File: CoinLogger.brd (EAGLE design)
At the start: 34.8 x 34.8 mm, 17 parts, among them IC1 TINY11S, U4 LIS331

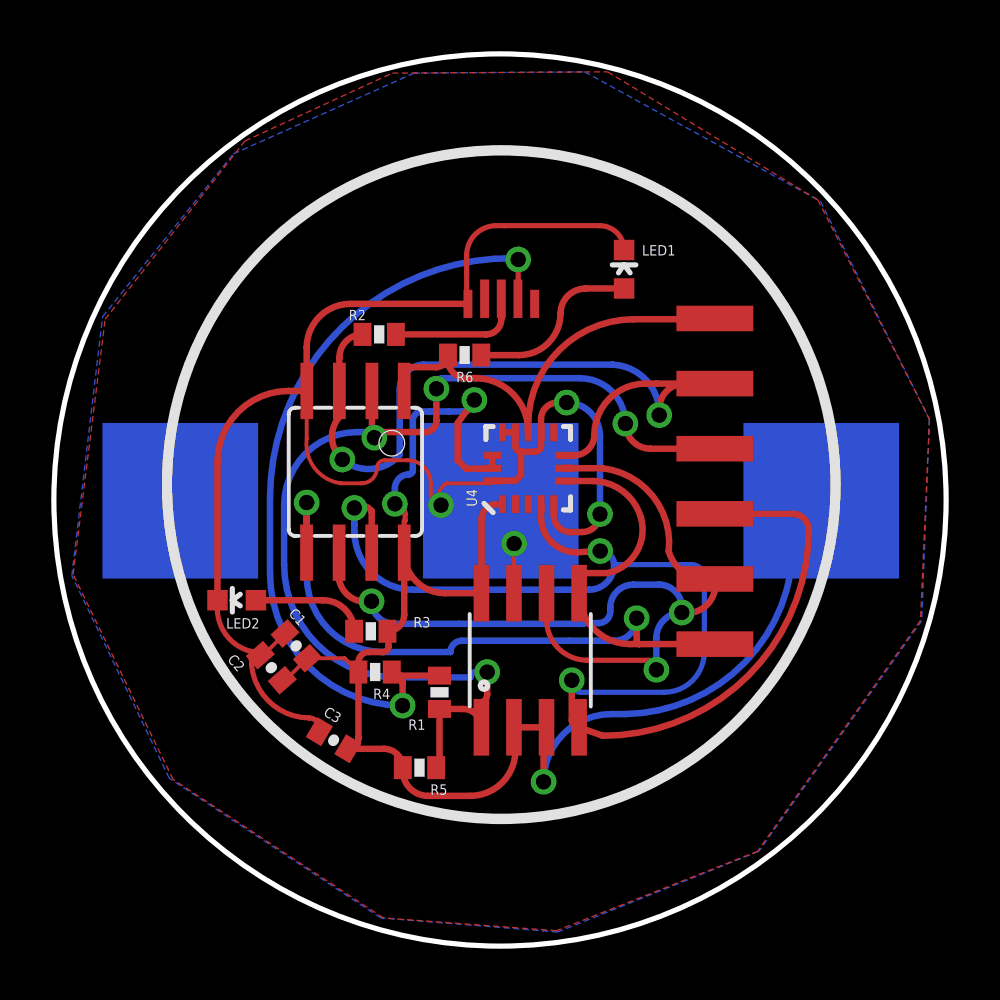
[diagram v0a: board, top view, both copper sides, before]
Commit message: Board is now v1.1
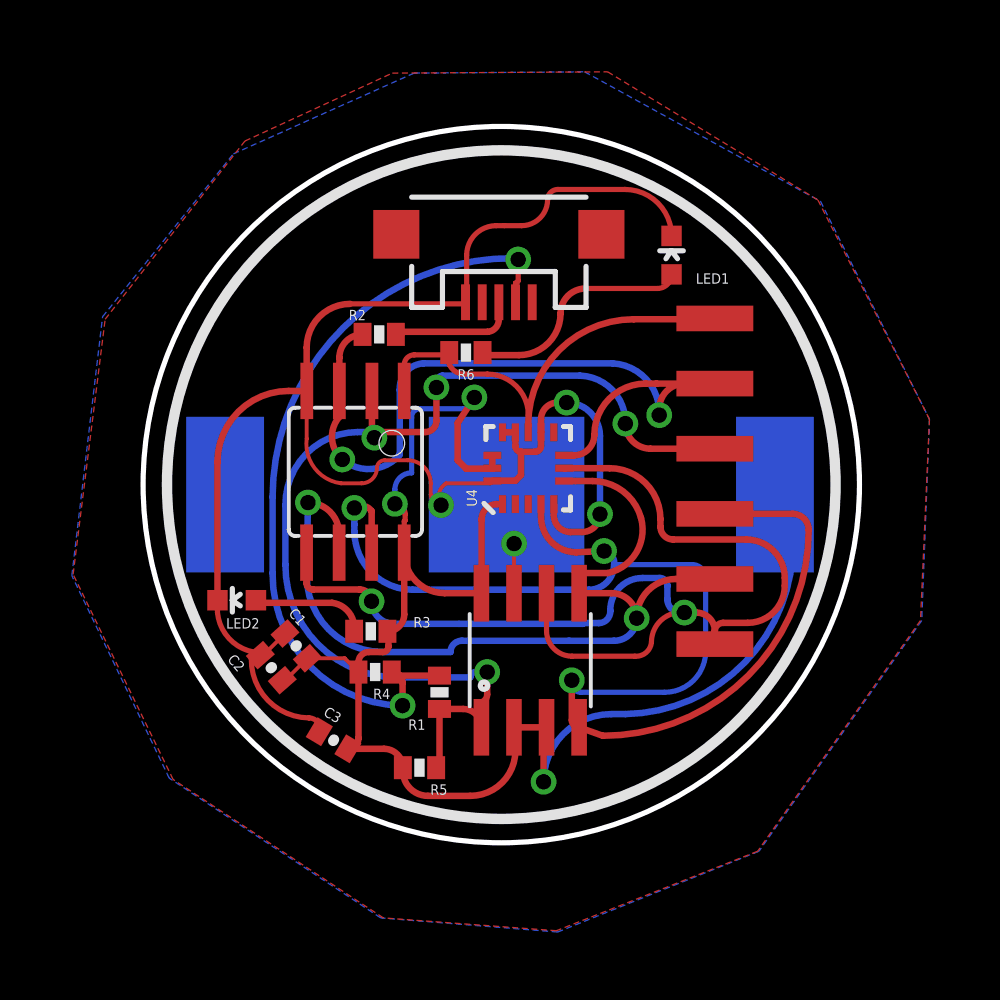
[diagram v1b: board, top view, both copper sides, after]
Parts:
- removed BAT2: (no value), SparkFun:BATTCON_20MM
- removed JP1: USB_MICROB_PLUG, SparkFun:MICRO-B-RA-SMT
- added BAT1: (no value), SparkFun:BATTCON_20MM
- added X1: USB-MICROB, SparkFun:USB-MICROB
- moved LED1 1.93 mm to (28.6, 46.0)
- moved R6 0.11 mm to (20.6, 42.2)
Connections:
- net GND: now also BAT1.2, X1.GND; no longer BAT2.2, JP1.5
- net N$2: now also X1.D+; no longer JP1.3
- net N$6: now also IC1.5, JP2.1; no longer IC1.6, JP2.2
- net N$7: now also IC1.6, JP2.2; no longer IC1.5, JP2.1
- net N$8: now also X1.D-; no longer JP1.2
- net VCC: now also BAT1.1; no longer BAT2.1
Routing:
- net N$6: track 34.9 -> 43.1 mm, vias 3 -> 2
- net N$10: track 6.65 -> 8.72 mm
- net VCC: track 61.1 -> 62.0 mm
- net N$12: track 17.5 -> 18.1 mm
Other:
- board size 34.8 x 34.8 mm -> 27.9 x 27.9 mm

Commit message: Lots of fixes, added NanoLogger
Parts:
- added R7: 4.7k, SparkFun:0402-RES
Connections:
- removed net N$11: IC1.3, JP2.5, R2.1, U4.8
- removed net N$12: IC1.1, JP2.6, R6.2, U4.11
- new net N$13: IC1.3, R1.1, R6.2
- new net N$9: IC1.1, R7.1
- net GND: now also JP2.5
- net N$4: now also R2.1, U4.8; no longer R1.1
- net N$6: now also U4.11
- net VCC: now also JP2.6, R7.2
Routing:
- net N$11: track 30.2 -> 0.00 mm, vias 2 -> 0
- net N$13: track 0.00 -> 27.4 mm, vias 0 -> 2
- net N$12: track 18.1 -> 0.00 mm
- net N$4: track 41.7 -> 38.6 mm
- net N$9: track 0.00 -> 2.96 mm
